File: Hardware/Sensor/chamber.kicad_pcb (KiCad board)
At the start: 2 copper layers, 83 x 95 mm, 106 parts, among them J1 Conn_01x16_Female, J2 Conn_01x16_Female, J3 RF_Shield_One_Piece, J4 Conn_Coaxial, J5 Conn_01x03_Male, J6 Conn_01x03_Male, J7 UART, J8 USB_B_Micro, J9 Conn_01x04, Q1 Q_PMOS_GDS, Q2 Q_PMOS_GDS, Q3 Q_NMOS_GDS, Q4 Q_NMOS_GDS, Q5 Q_NPN_BEC, Q6 Q_PMOS_GDS, Q7 Q_NMOS_GDS, Q8 Q_PMOS_GDS, Q9 Q_NMOS_GDS, SW1 UP, SW2 DOWN, SW3 LEFT, SW4 RIGHT, U1 SSD1306, U2 MCP3425A0T-ECH, U3 LMC662, U4 LM358, U5 STM8S105K4B6, Y1 Crystal

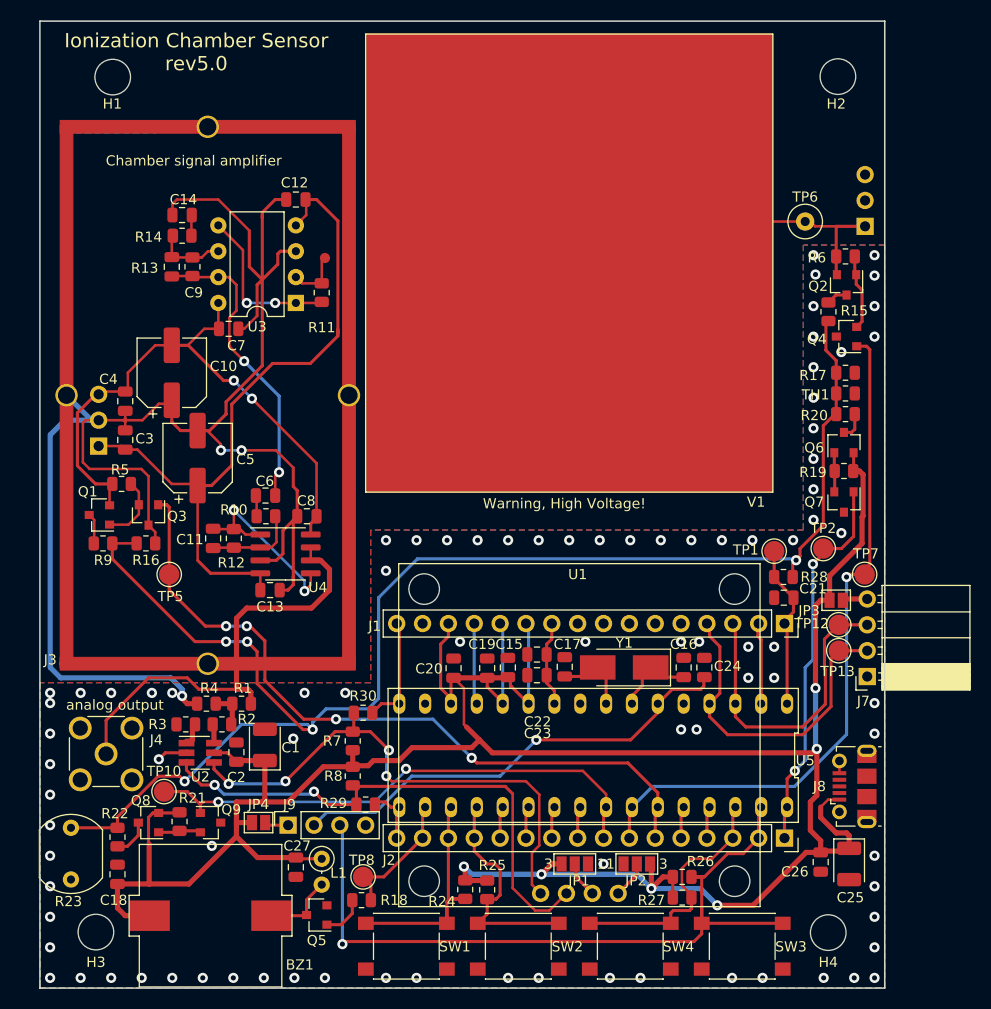
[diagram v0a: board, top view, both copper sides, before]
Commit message: this is what was send for pcb production
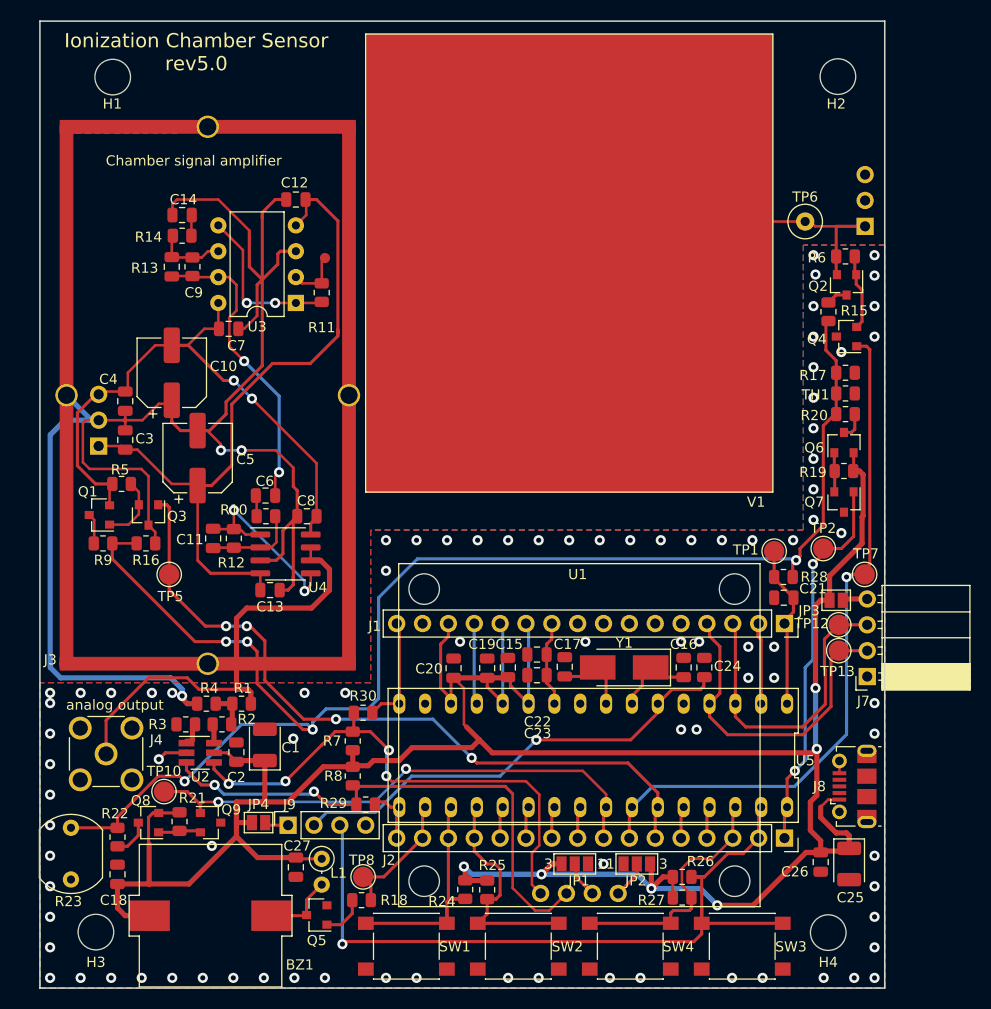
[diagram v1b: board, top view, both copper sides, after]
